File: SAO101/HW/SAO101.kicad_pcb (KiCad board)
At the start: 2 copper layers, 48 x 48 mm, 46 parts, among them J1 USB_B_Micro, J2 SAO_Conn, U1 AMS1117-3.3, U2 MCP23017_SS

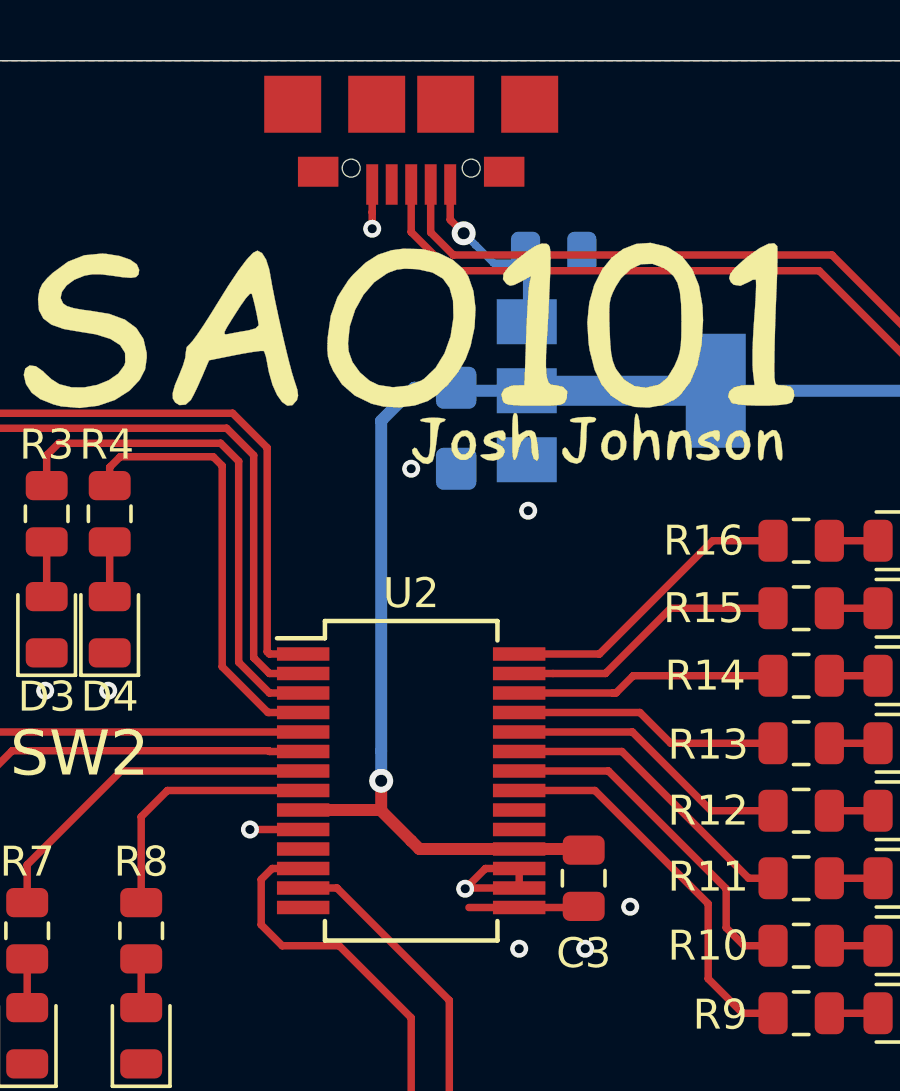
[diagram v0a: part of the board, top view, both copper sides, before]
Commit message: added more slides and resources, small routing changes
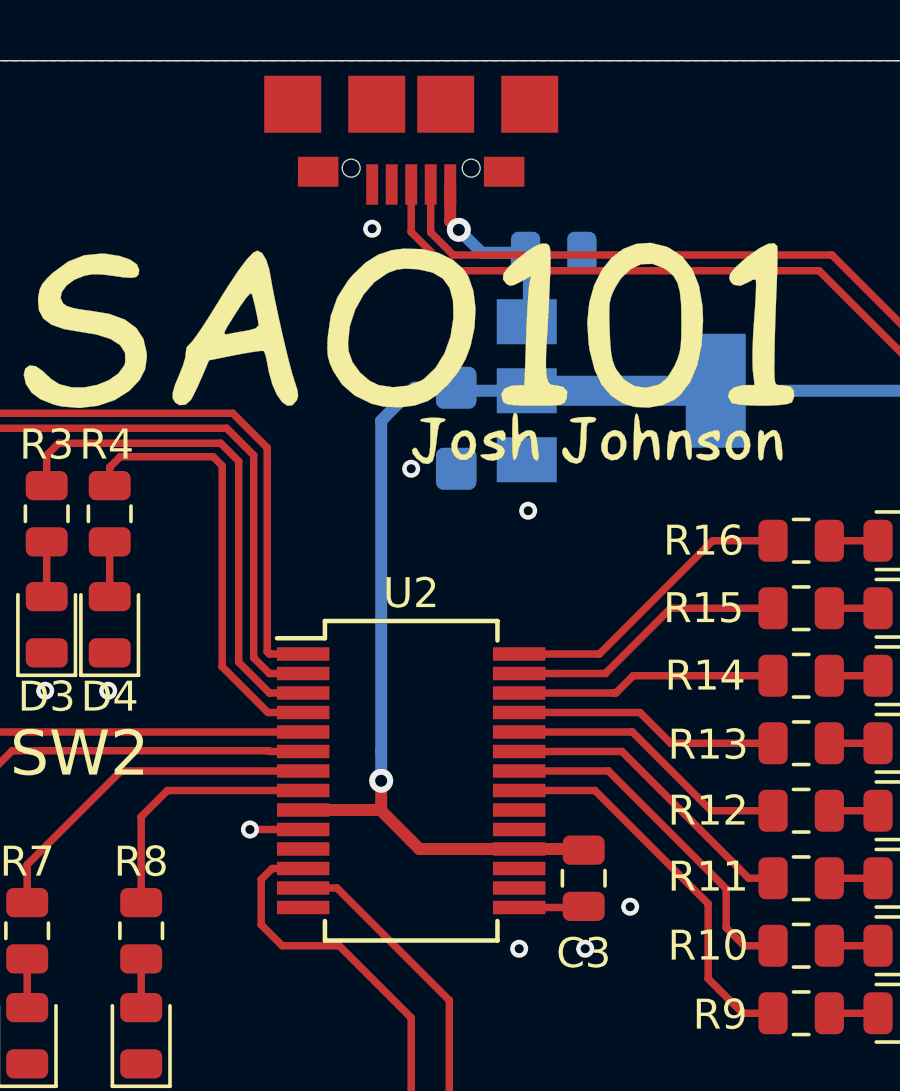
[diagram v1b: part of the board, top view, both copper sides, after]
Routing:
- net GND: track 11.6 -> 3.94 mm, vias 24 -> 23
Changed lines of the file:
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@@
     (thickness 1.6)
     (drawings 14)
-    (tracks 186)
+    (tracks 175)
     (zones 0)
     (modules 46)
@@
   (setup
     (last_trace_width 0.25)
+    (user_trace_width 0.25)
+    (user_trace_width 0.5)
     (trace_clearance 0.2)
-    (zone_clearance 0.508)
+    (zone_clearance 0.3)
     (zone_45_only no)
     (trace_min 0.2)
@@
   (segment (start 130.85 66.7875) (end 130.8125 66.75) (width 0.25) (layer B.Cu) (net 1))
   (segment (start 130.85 68.7) (end 130.85 66.7875) (width 0.25) (layer B.Cu) (net 1))
-  (segment (start 128.3 65.3) (end 128.350001 65.350001) (width 0.25) (layer F.Cu) (net 1))
-  (segment (start 129.75 66.75) (end 129.149999 66.149999) (width 0.25) (layer B.Cu) (net 1))
-  (segment (start 128.3 64.125) (end 128.3 65.3) (width 0.25) (layer F.Cu) (net 1))
-  (segment (start 129.149999 66.149999) (end 128.75 65.75) (width 0.25) (layer B.Cu) (net 1))
-  (segment (start 130.8125 66.75) (end 129.75 66.75) (width 0.25) (layer B.Cu) (net 1))
-  (segment (start 128.350001 65.350001) (end 128.75 65.75) (width 0.25) (layer F.Cu) (net 1))
-  (via (at 128.75 65.75) (size 0.8) (drill 0.4) (layers F.Cu B.Cu) (net 1))
+  (via (at 128.588652 65.636348) (size 0.8) (drill 0.4) (layers F.Cu B.Cu) (net 1))
+  (segment (start 130.8125 66.4) (end 129.352304 66.4) (width 0.4) (layer B.Cu) (net 1))
+  (segment (start 129.352304 66.4) (end 128.588652 65.636348) (width 0.4) (layer B.Cu) (net 1))
+  (segment (start 128.3 65.347696) (end 128.588652 65.636348) (width 0.4) (layer F.Cu) (net 1))
+  (segment (start 128.3 64.125) (end 128.3 65.347696) (width 0.4) (layer F.Cu) (net 1))
   (segment (start 123.4 85.625) (end 121.625 85.625) (width 0.25) (layer F.Cu) (net 2))
-  (segment (start 130.6 86.925) (end 130.6 87.575) (width 0.25) (layer F.Cu) (net 2))
   (segment (start 132.7125 88.225) (end 132.75 88.1875) (width 0.25) (layer F.Cu) (net 2))
   (segment (start 130.6 88.225) (end 132.7125 88.225) (width 0.25) (layer F.Cu) (net 2))
-  (segment (start 125.7 64.125) (end 125.7 65.05) (width 0.25) (layer F.Cu) (net 2))
-  (segment (start 125.7 65.05) (end 125.7 65.6) (width 0.25) (layer F.Cu) (net 2))
   (via (at 145.8 76) (size 0.6) (drill 0.3) (layers F.Cu B.Cu) (net 2))
   (via (at 145.8 78.3) (size 0.6) (drill 0.3) (layers F.Cu B.Cu) (net 2))
@@
   (segment (start 121.625 85.625) (end 121.625 85.625) (width 0.25) (layer F.Cu) (net 2))
   (via (at 121.625 85.625) (size 0.6) (drill 0.3) (layers F.Cu B.Cu) (net 2))
-  (via (at 128.8 87.6) (size 0.6) (drill 0.3) (layers F.Cu B.Cu) (net 2))
-  (segment (start 128.825 87.575) (end 128.8 87.6) (width 0.25) (layer F.Cu) (net 2))
-  (segment (start 130.6 87.575) (end 128.825 87.575) (width 0.25) (layer F.Cu) (net 2))
-  (segment (start 130.6 88.225) (end 128.925 88.225) (width 0.25) (layer F.Cu) (net 2))
-  (segment (start 129.475 86.925) (end 128.8 87.6) (width 0.25) (layer F.Cu) (net 2))
-  (segment (start 130.6 86.925) (end 129.475 86.925) (width 0.25) (layer F.Cu) (net 2))
   (segment (start 125.7 65.6) (end 125.7 65.6) (width 0.25) (layer F.Cu) (net 2))
   (via (at 125.7 65.6) (size 0.6) (drill 0.3) (layers F.Cu B.Cu) (net 2))
@@
   (segment (start 133.275 79.775) (end 137.05 76) (width 0.25) (layer F.Cu) (net 37))
   (zone (net 2) (net_name GND) (layer F.Cu) (hatch edge 0.508)
-    (connect_pads (clearance 0.508))
+    (connect_pads (clearance 0.3))
     (min_thickness 0.2)
-    (fill yes (arc_segments 32) (thermal_gap 0.508) (thermal_bridge_width 0.508))
+    (fill yes (arc_segments 32) (thermal_gap 0.21) (thermal_bridge_width 0.21))
     (polygon
       (pts
